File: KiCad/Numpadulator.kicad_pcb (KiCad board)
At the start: 2 copper layers, 81.3 x 138.4 mm, 61 parts, among them SW1 Cherry_MX_RGB_WS2812, SW10 Cherry_MX_RGB_WS2812, SW11 Cherry_MX_RGB_WS2812, SW12 Cherry_MX_RGB_WS2812, SW13 Cherry_MX_RGB_WS2812, SW14 Cherry_MX_RGB_WS2812, SW15 Cherry_MX_RGB_WS2812, SW16 Cherry_MX_RGB_WS2812, SW19 Rotary_Encoder_Switch, SW2 Cherry_MX_RGB_WS2812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

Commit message: Actually made the thing symmetric
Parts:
- moved U2 0.64 mm to (101.0, 69.8)
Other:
- board size 81.3 x 138.4 mm -> 82.6 x 138.4 mm

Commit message: fixed track
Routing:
- net LED: track 60.4 -> 59.9 mm
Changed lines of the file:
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@@
   (segment (start 60.96 61.994) (end 60.9 61.934) (width 0.254) (layer B.Cu) (net 31))
   (segment (start 60.96 63.754) (end 60.96 61.994) (width 0.254) (layer B.Cu) (net 31))
-  (segment (start 101.6 38.1) (end 99.822 36.322) (width 0.254) (layer B.Cu) (net 32))
   (via (at 73.152 36.322) (size 0.8) (drill 0.4) (layers F.Cu B.Cu) (net 32))
-  (segment (start 99.822 36.322) (end 73.914 36.322) (width 0.254) (layer B.Cu) (net 32))
   (via (at 73.152 60.452) (size 0.8) (drill 0.4) (layers F.Cu B.Cu) (net 32))
   (segment (start 73.152 36.322) (end 73.152 60.452) (width 0.254) (layer F.Cu) (net 32))
   (segment (start 66.1455 60.452) (end 66.1 60.4975) (width 0.254) (layer B.Cu) (net 32))
   (segment (start 73.152 60.452) (end 66.1455 60.452) (width 0.254) (layer B.Cu) (net 32))
-  (segment (start 73.914 36.322) (end 73.152 36.322) (width 0.254) (layer B.Cu) (net 32))
+  (segment (start 73.152 36.322) (end 99.822 36.322) (width 0.254) (layer B.Cu) (net 32))
+  (segment (start 99.822 37.592) (end 100.33 38.1) (width 0.254) (layer B.Cu) (net 32))
+  (segment (start 99.822 36.322) (end 99.822 37.592) (width 0.254) (layer B.Cu) (net 32))
   (via (at 60.96 91.44) (size 0.8) (drill 0.4) (layers F.Cu B.Cu) (net 33))
   (segment (start 60.9 91.38) (end 60.96 91.44) (width 0.254) (layer B.Cu) (net 33))

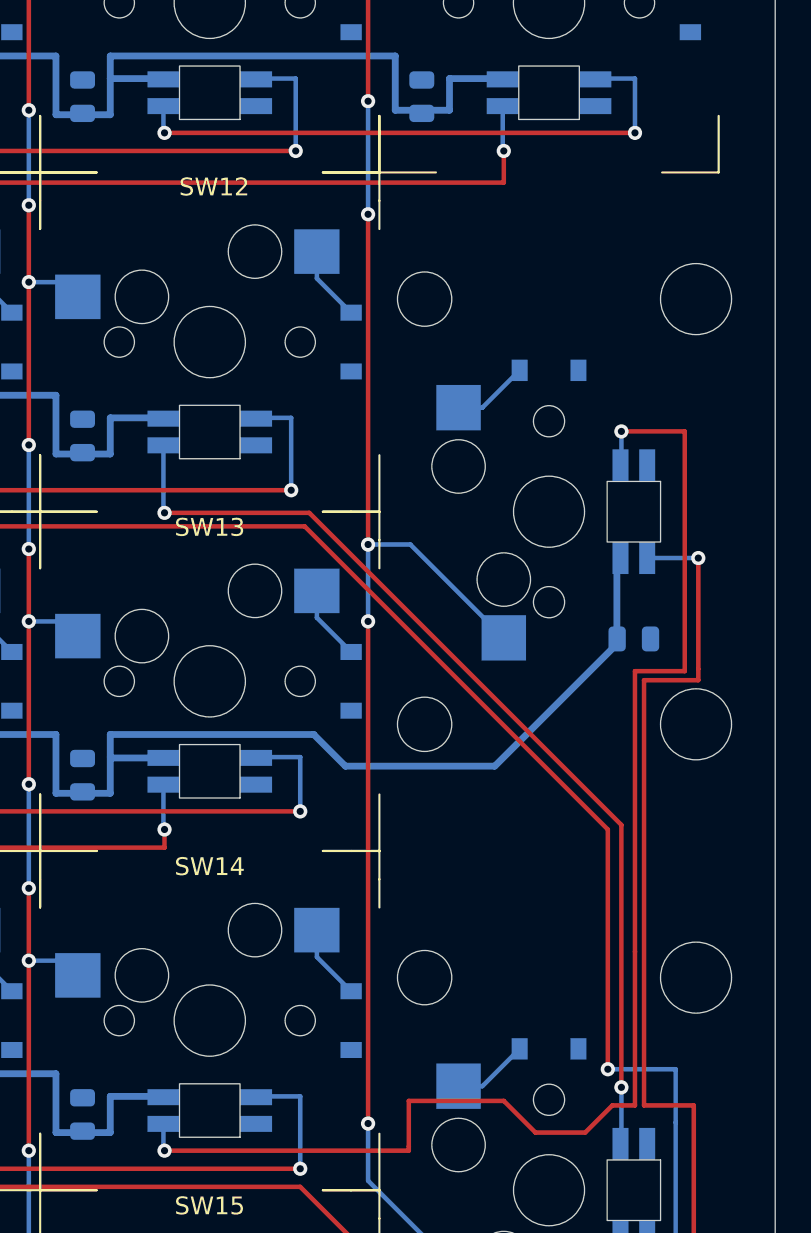
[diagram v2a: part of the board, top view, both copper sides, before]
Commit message: flipped top right 1.5u. now the bottom right...
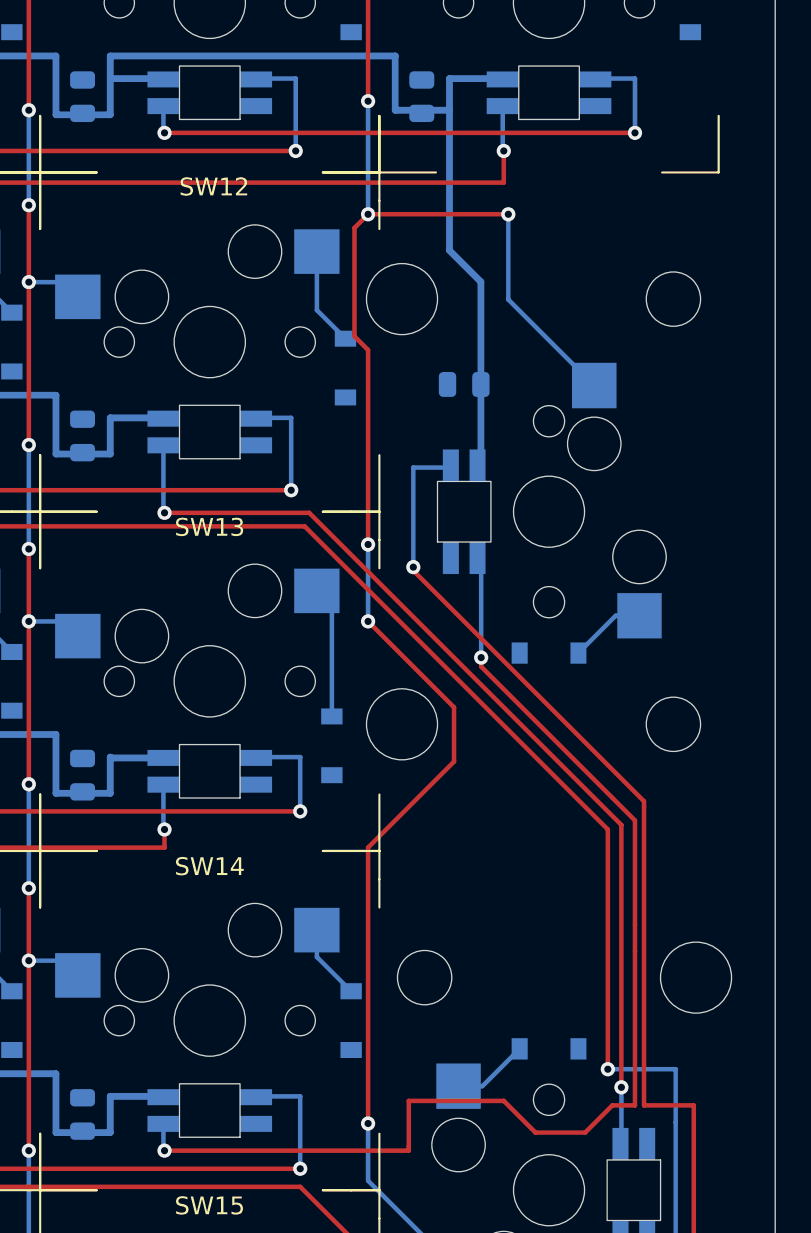
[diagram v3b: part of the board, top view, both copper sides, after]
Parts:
- moved C17 17.2 mm to (115.9, 105.6), turned to 180 degrees
- moved D18 15.9 mm to (120.7, 120.7), turned to 0 degrees
- moved D22 9.52 mm to (115.9, 112.7), turned to 270 degrees
- moved D13 3.78 mm to (108.5, 125.9)
- moved D12 1.49 mm to (109.2, 104.6)
- turned MX3 to 270 degrees
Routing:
- net VCC: track 603.6 -> 586.5 mm
- net COL3: track 132.7 -> 147.0 mm, vias 7 -> 8
- net Net-(D22-Pad4): track 78.1 -> 66.5 mm
- net Net-(D20-Pad4): track 123.8 -> 130.4 mm
- net Net-(D13-Pad2): track 4.23 -> 7.40 mm
- net Net-(D12-Pad2): track 4.23 -> 5.56 mm

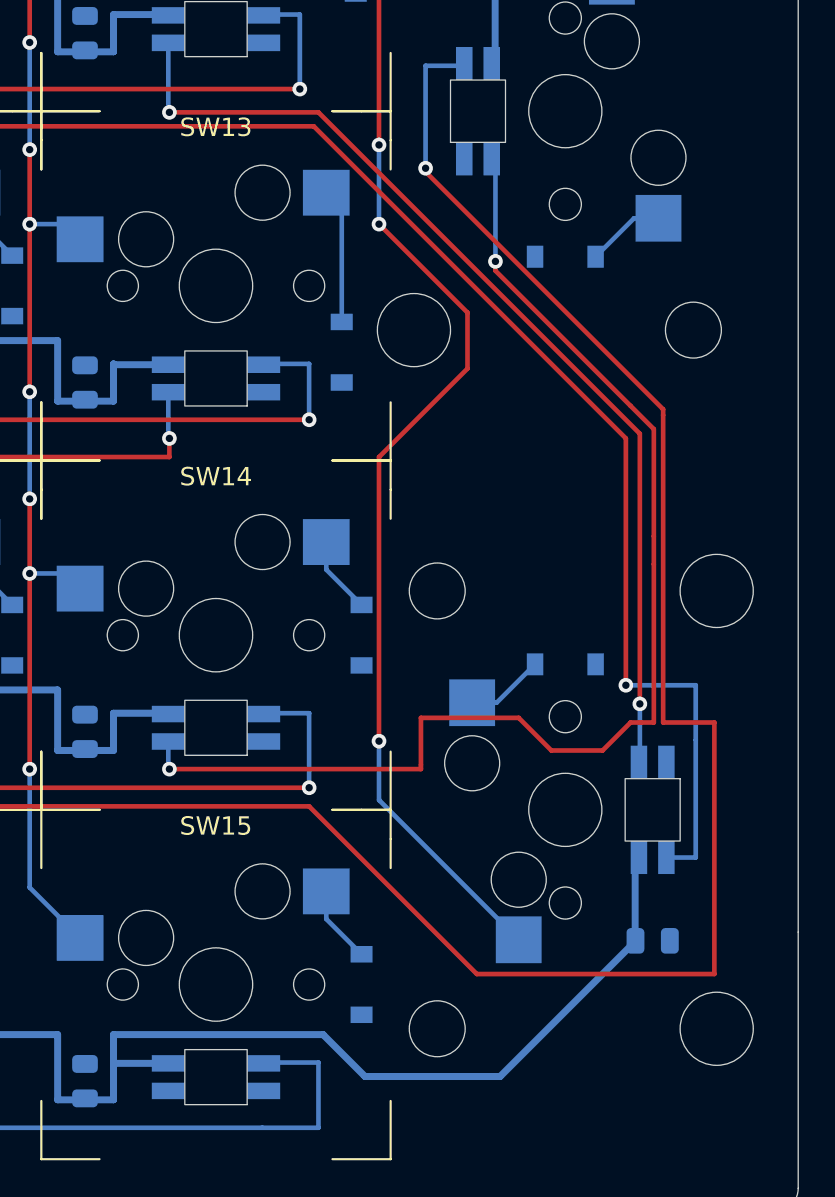
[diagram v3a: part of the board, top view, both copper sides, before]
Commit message: flipped the side 1.5us. ugh.
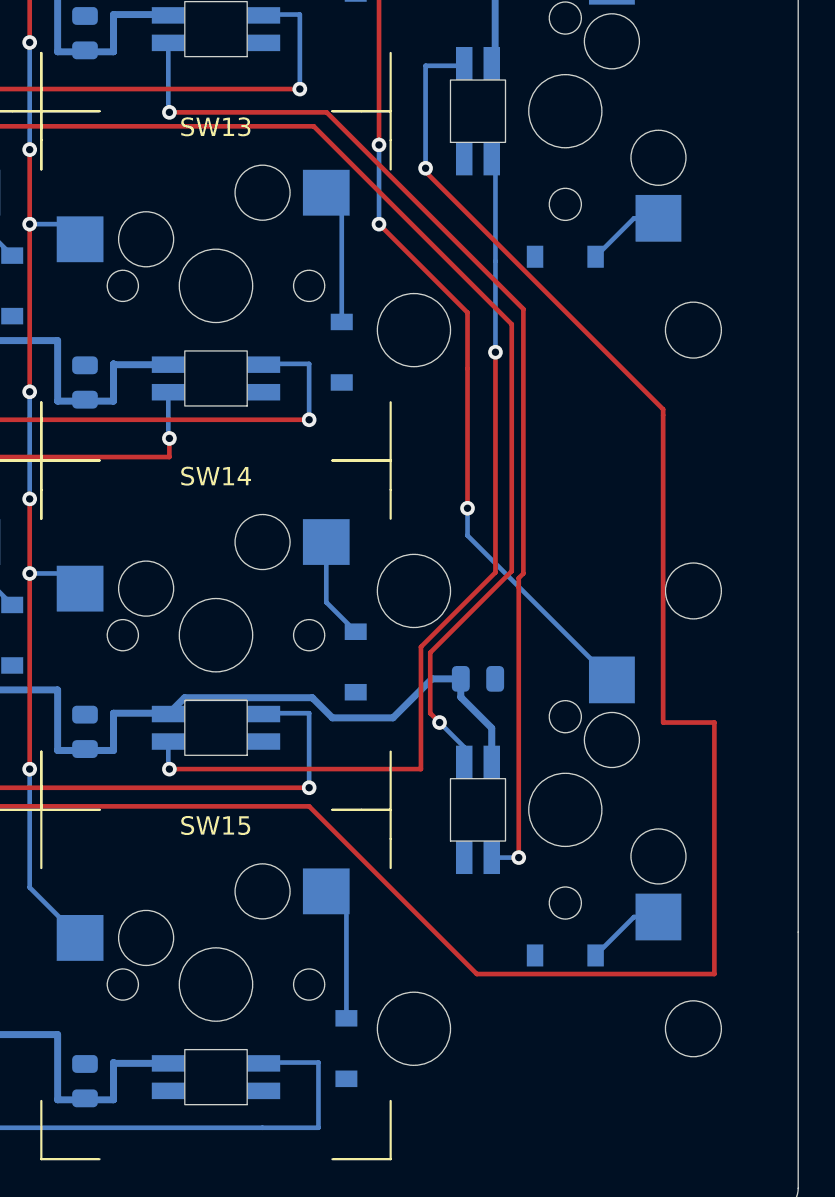
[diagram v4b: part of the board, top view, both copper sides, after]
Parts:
- moved C18 17.2 mm to (115.9, 143.7)
- moved D17 15.9 mm to (120.7, 158.8), turned to 0 degrees
- moved D21 9.52 mm to (115.9, 150.8), turned to 270 degrees
- moved D15 3.59 mm to (108.7, 163.8)
- moved D14 1.49 mm to (109.2, 142.7)
- turned MX2 to 270 degrees
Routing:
- net Net-(D22-Pad4): track 66.5 -> 50.3 mm
- net COL3: track 147.0 -> 130.9 mm
- net VCC: track 586.5 -> 571.1 mm
- net Net-(D21-Pad2): track 105.9 -> 95.3 mm
- net Net-(D21-Pad4): track 54.8 -> 59.1 mm
- net Net-(D15-Pad2): track 4.23 -> 8.12 mm
- net Net-(D14-Pad2): track 4.23 -> 5.56 mm

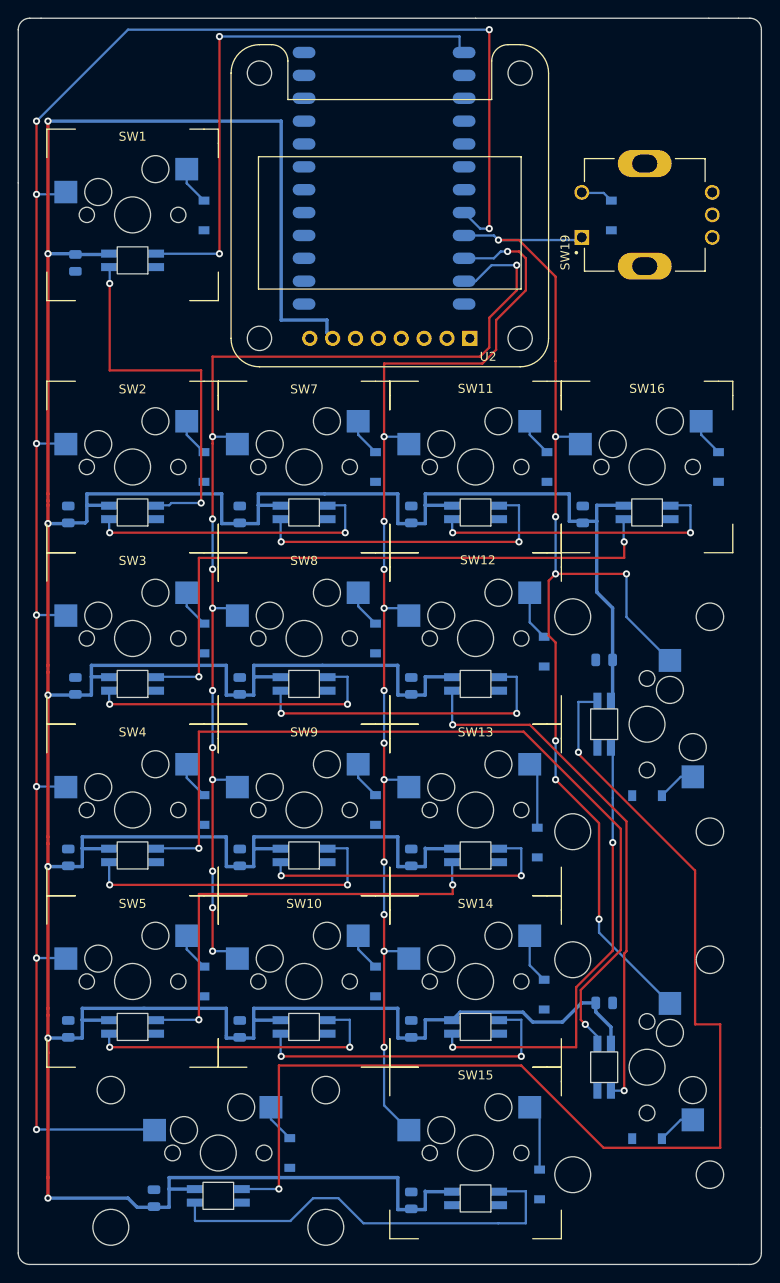
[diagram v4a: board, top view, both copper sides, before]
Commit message: Wired up rows, realized there is something wrong with the 2u keys rows in the schematic...
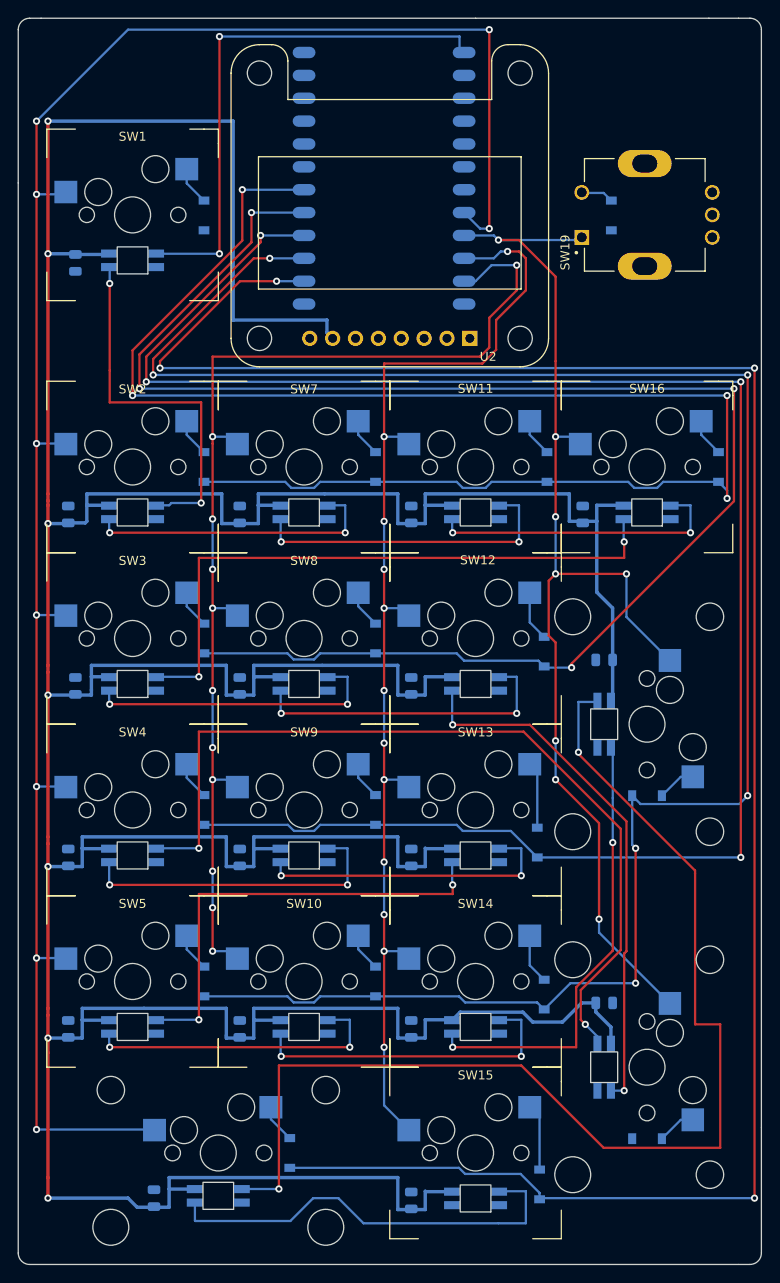
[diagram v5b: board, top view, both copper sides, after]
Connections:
- D12 pad 1: Net-(D12-Pad1) -> ROW2
- D14 pad 1: Net-(D14-Pad1) -> ROW4
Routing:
- net ROW5: track 0.00 -> 232.2 mm, vias 0 -> 4
- net ROW4: track 0.00 -> 220.8 mm, vias 0 -> 6
- net ROW3: track 0.00 -> 206.9 mm, vias 0 -> 4
- net ROW2: track 0.00 -> 177.1 mm, vias 0 -> 4
- net ROW1: track 0.00 -> 173.3 mm, vias 0 -> 4

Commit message: Switched + and return to be in right order and orientation...also maybe finished routing??
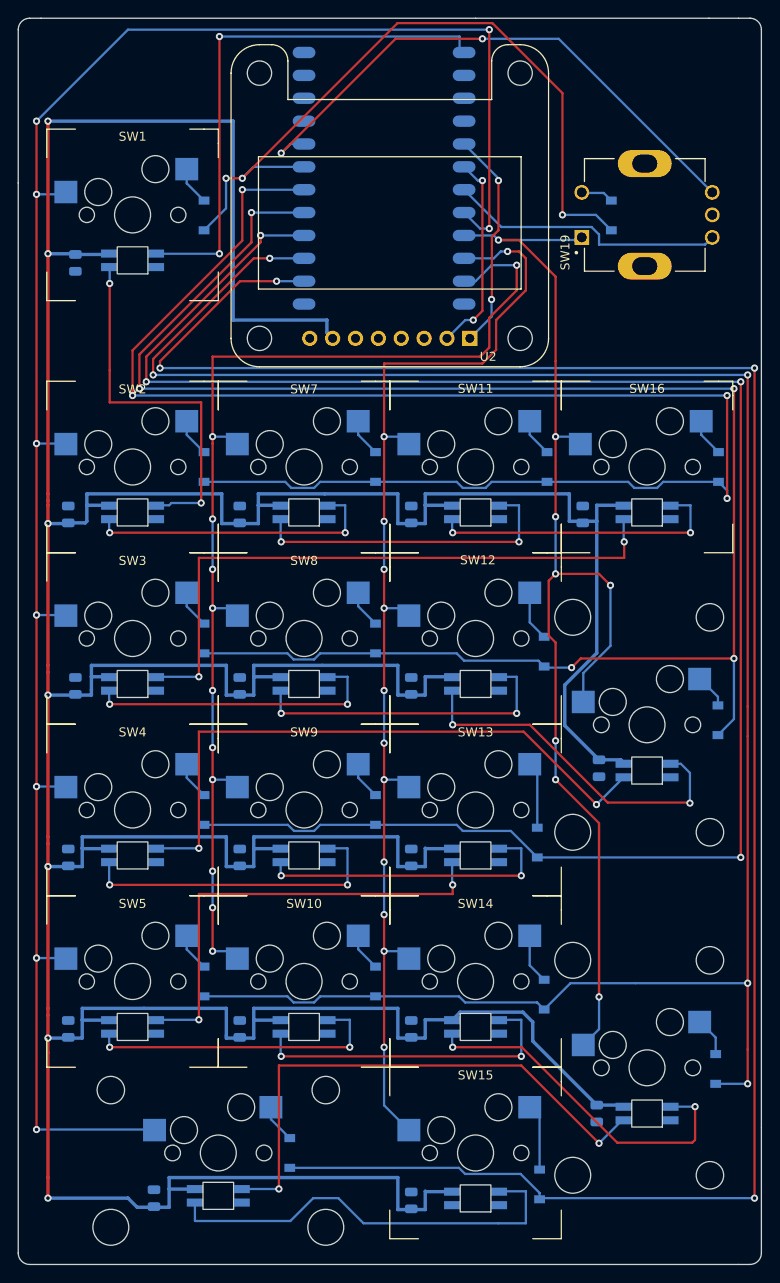
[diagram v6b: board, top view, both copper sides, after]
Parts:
- moved D17 47.1 mm to (128.5, 112.3), turned to 90 degrees
- moved D22 43.5 mm to (120.7, 156.0), turned to 0 degrees
- moved MX3 38.2 mm to (120.7, 150.9)
- moved MX2 38.0 mm to (120.7, 112.8)
- moved D21 33.3 mm to (120.7, 117.9), turned to 0 degrees
- moved D18 31.3 mm to (128.3, 151.0), turned to 90 degrees
- moved C18 12.3 mm to (115.1, 156.0), turned to 270 degrees
- moved C17 12.0 mm to (115.3, 117.6), turned to 270 degrees
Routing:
- net ROW0: track 0.00 -> 81.6 mm, vias 0 -> 3
- net Net-(D20-Pad4): track 130.4 -> 60.7 mm
- net ROTB: track 0.00 -> 63.2 mm, vias 0 -> 2
- net ROTA: track 0.00 -> 31.1 mm
- net Net-(D21-Pad2): track 95.3 -> 69.3 mm
- net SDA: track 0.00 -> 24.5 mm, vias 0 -> 2
- net SCL: track 0.00 -> 22.3 mm, vias 0 -> 2
- net ROW2: track 177.1 -> 196.5 mm, vias 4 -> 5
- net Net-(D21-Pad4): track 59.1 -> 39.7 mm
- net VCC: track 571.1 -> 584.9 mm
- net ROW4: track 220.8 -> 234.3 mm, vias 6 -> 5
- net Net-(D22-Pad4): track 50.3 -> 39.4 mm
- net COL3: track 130.9 -> 134.3 mm

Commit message: FINISHED THE WIRING except now I need to add the underglow LEDs...
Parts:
- moved C2 0.54 mm to (56.9, 89.4), turned to 270 degrees
- turned C10 to 270 degrees
- turned C11 to 270 degrees
- turned C12 to 270 degrees
- turned C13 to 270 degrees
- turned C14 to 270 degrees
- turned C15 to 270 degrees
- turned C16 to 270 degrees
- turned C3 to 270 degrees
- turned C4 to 270 degrees
- turned C5 to 270 degrees
- turned C6 to 270 degrees
- turned C7 to 270 degrees
- turned C8 to 270 degrees
- turned C9 to 270 degrees
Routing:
- net VCC: track 584.9 -> 545.4 mm
- net Net-(D20-Pad2): vias 0 -> 2
